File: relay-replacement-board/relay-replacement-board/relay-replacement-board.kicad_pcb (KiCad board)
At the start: 2 copper layers, 100 x 55 mm, 27 parts, among them J1 Conn_01x02, J10 Conn_01x02, J11 Conn_01x02, J12 Conn_01x02, J13 Conn_01x02, J2 Conn_01x02, J3 Conn_01x02, J4 Conn_01x02, J5 Conn_01x02, J6 Conn_01x02, J7 Conn_01x02, J8 Conn_01x02, J9 Conn_01x02, Q1 NVD5865NL, Q2 NVD5865NL, Q3 NVD5865NL, Q4 NVD5865NL, Q5 NVD5865NL, Q6 NVD5865NL, Q7 NVD5865NL

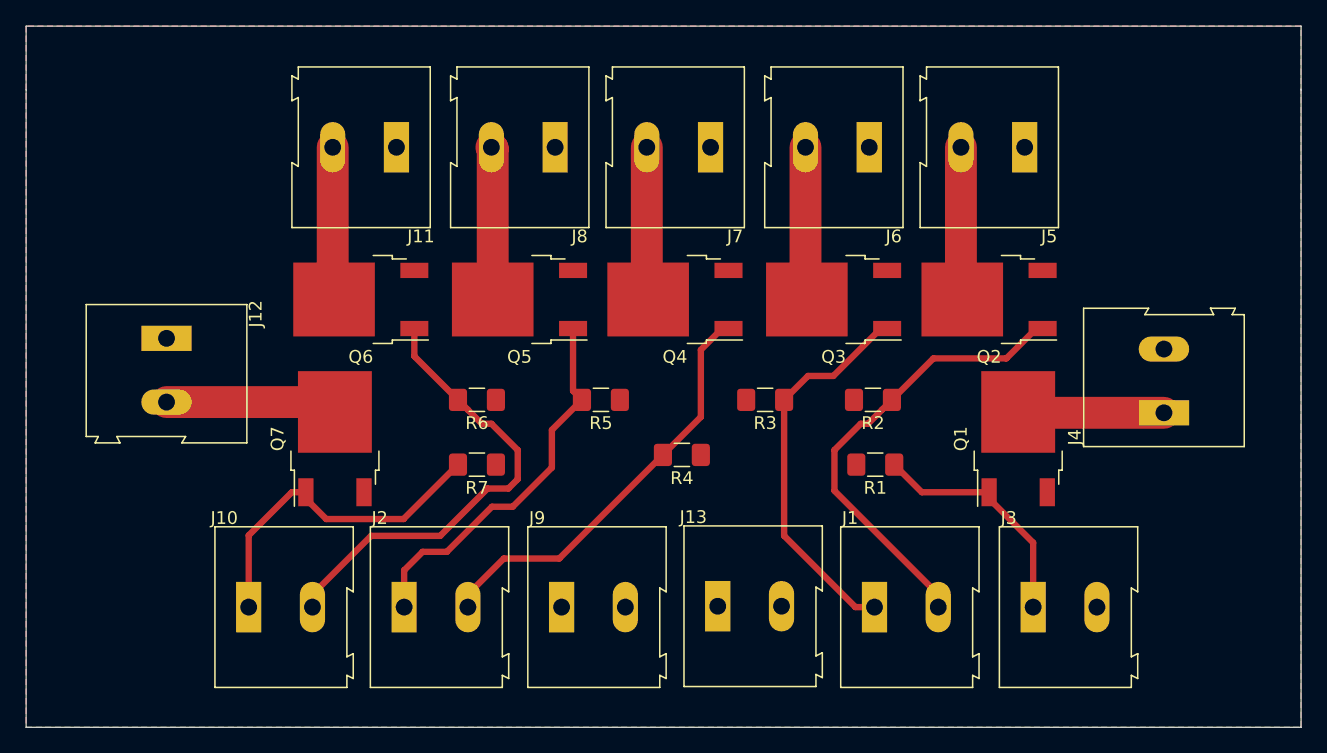
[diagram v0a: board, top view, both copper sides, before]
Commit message: Added flyback diodes
These protect the MOSFETs when they switch off. PCB also reorganised and shrunk slightly to 10*5cm
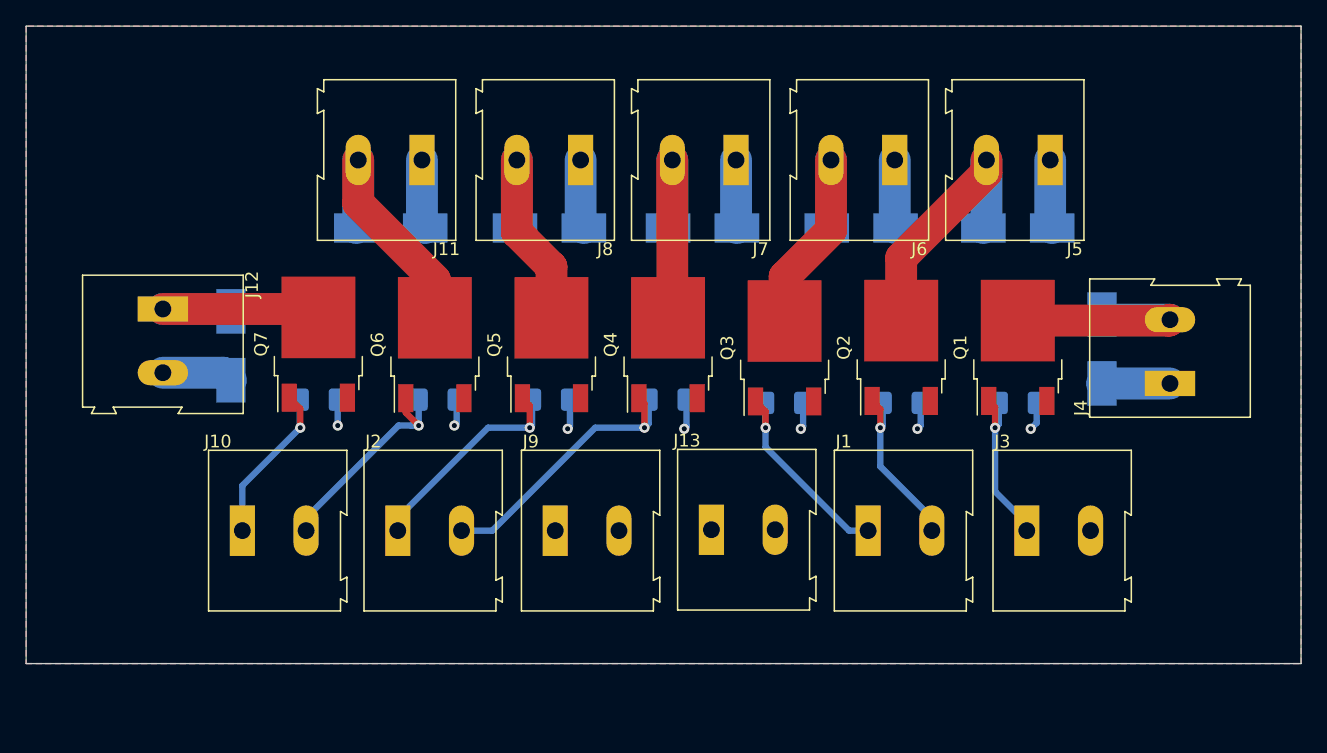
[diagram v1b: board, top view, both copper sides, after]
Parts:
- added D1: D, Diode_SMD:D_SMB_Handsoldering, B.Cu at (169.4, 95.3)
- added D2: D, Diode_SMD:D_SMB_Handsoldering, B.Cu at (162.8, 85.8)
- added D3: D, Diode_SMD:D_SMB_Handsoldering, B.Cu at (150.5, 85.8)
- added D4: D, Diode_SMD:D_SMB_Handsoldering, B.Cu at (138.1, 85.8)
- added D5: D, Diode_SMD:D_SMB_Handsoldering, B.Cu at (126.0, 85.8)
- added D6: D, Diode_SMD:D_SMB_Handsoldering, B.Cu at (113.6, 85.8)
- added D7: D, Diode_SMD:D_SMB_Handsoldering, B.Cu at (101.1, 95.1)
- R1, R2, R3, R4, R5, R6, R7: moved to B.Cu
- moved R7 13.4 mm to (108.0, 99.3)
- moved R1 12.2 mm to (162.8, 99.6)
- moved Q2 7.85 mm to (153.6, 95.2), turned to 90 degrees
- moved Q7 7.53 mm to (107.9, 94.9)
- moved Q1 7.16 mm to (162.8, 95.2)
- moved Q6 6.80 mm to (117.1, 95.0), turned to 90 degrees
- moved J1 6.02 mm to (151.0, 109.6)
- moved J10 6.02 mm to (102.0, 109.6)
- moved J13 6.02 mm to (138.8, 109.5)
- moved J2 6.02 mm to (114.2, 109.6)
- moved J3 6.02 mm to (163.5, 109.6)
- moved J9 6.02 mm to (126.5, 109.6)
- moved Q3 5.40 mm to (144.5, 95.2), turned to 90 degrees
- moved R4 4.48 mm to (135.3, 99.3)
- moved Q5 4.34 mm to (126.2, 95.0), turned to 90 degrees
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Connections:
- J12 pad 1: +12V -> Net-(D7-Pad2)
- J12 pad 2: Net-(J12-Pad2) -> +12V
- J4 pad 1: Net-(J4-Pad1) -> +12V
- J4 pad 2: +12V -> Net-(D1-Pad2)
- Q1 pad 2: Net-(J4-Pad1) -> Net-(D1-Pad2)
- Q7 pad 2: Net-(J12-Pad2) -> Net-(D7-Pad2)
- R1 pad 1: /trigger0 -> GND
- R1 pad 2: GND -> /trigger0
- R2 pad 1: /trigger1 -> GND
- R2 pad 2: GND -> /trigger1
- R3 pad 1: /trigger2 -> GND
- R3 pad 2: GND -> /trigger2
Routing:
- net +12V: track 0.00 -> 37.9 mm
- net /trigger1: track 36.0 -> 14.1 mm, vias 0 -> 1
- net /trigger5: track 36.5 -> 17.4 mm, vias 0 -> 1
- net Net-(D7-Pad2): track 0.00 -> 17.9 mm
- net Net-(D1-Pad2): track 0.00 -> 17.5 mm
- net GND: track 0.00 -> 15.3 mm, vias 0 -> 7
- net /trigger2: track 30.5 -> 16.6 mm, vias 0 -> 1
- net Net-(J12-Pad2): track 13.5 -> 0.00 mm
- net /trigger6: track 26.4 -> 14.9 mm, vias 0 -> 1
- net Net-(J4-Pad1): track 11.5 -> 0.00 mm
- net /trigger4: track 31.0 -> 20.1 mm, vias 0 -> 1
- net /trigger3: track 33.2 -> 22.5 mm, vias 0 -> 1
- net Net-(D2-Pad2): track 12.0 -> 20.8 mm
- net Net-(D6-Pad2): track 12.0 -> 20.3 mm
- net Net-(D3-Pad2): track 12.0 -> 19.8 mm
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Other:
- board size 100 x 55 mm -> 100 x 50 mm

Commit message: Added M4 mounting holes
THese are not currently connected to Ground but could be
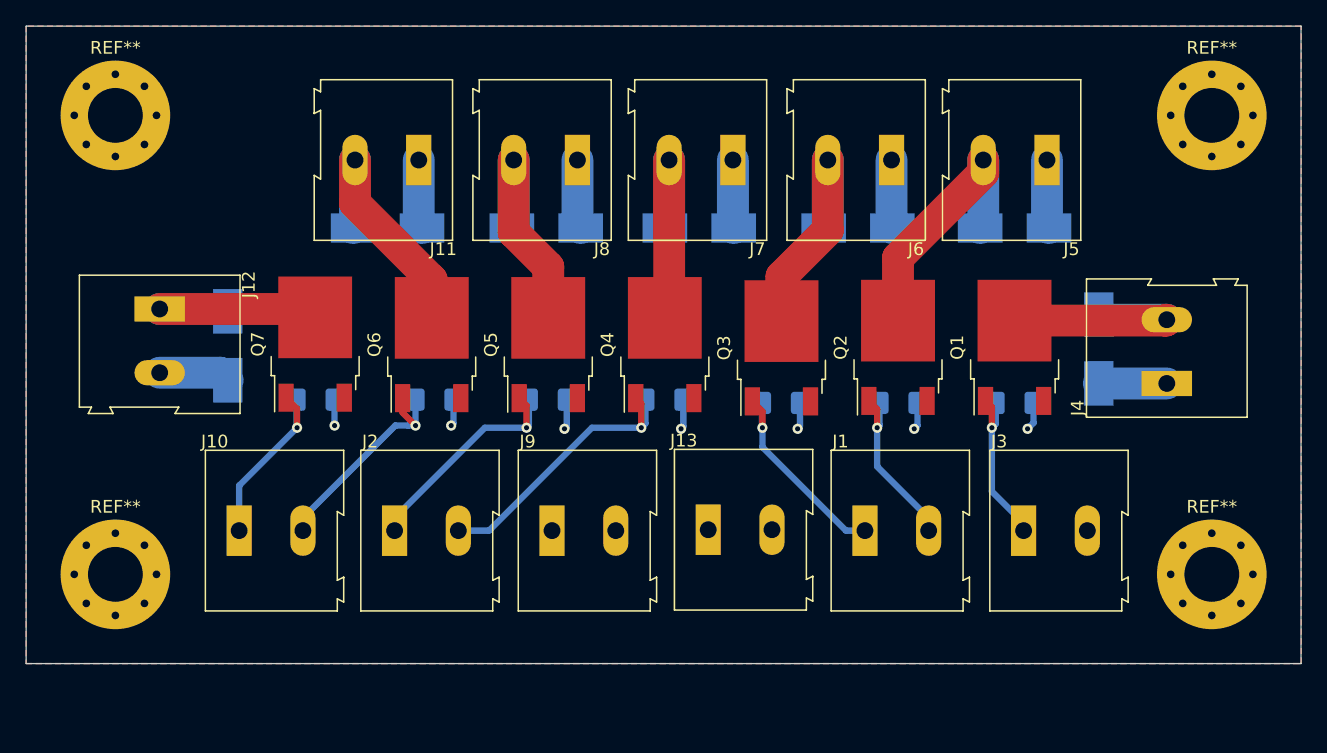
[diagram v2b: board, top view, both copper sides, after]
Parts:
- added REF**: MountingHole_4.3mm_M4_Pad_Via, MountingHole:MountingHole_4.3mm_M4_Pad_Via, F.Cu at (92.0, 77.0)
- added REF**: MountingHole_4.3mm_M4_Pad_Via, MountingHole:MountingHole_4.3mm_M4_Pad_Via, F.Cu at (178.0, 77.0)
- added REF**: MountingHole_4.3mm_M4_Pad_Via, MountingHole:MountingHole_4.3mm_M4_Pad_Via, F.Cu at (92.0, 113.0)
- added REF**: MountingHole_4.3mm_M4_Pad_Via, MountingHole:MountingHole_4.3mm_M4_Pad_Via, F.Cu at (178.0, 113.0)
- moved D1 0.25 mm to (169.1, 95.3)
- moved D2 0.25 mm to (162.5, 85.8)
- moved D3 0.25 mm to (150.2, 85.8)
- moved D4 0.25 mm to (137.8, 85.8)
- moved D5 0.25 mm to (125.8, 85.8)
- moved D6 0.25 mm to (113.3, 85.8)
- moved D7 0.25 mm to (100.8, 95.1)
- moved J1 0.25 mm to (150.8, 109.6)
- moved J10 0.25 mm to (101.7, 109.6)
- moved J11 0.25 mm to (115.8, 80.5)
- moved J12 0.25 mm to (95.5, 92.2)
- moved J13 0.25 mm to (138.5, 109.5)
- moved J2 0.25 mm to (113.9, 109.6)
- moved J3 0.25 mm to (163.2, 109.6)
- moved J4 0.25 mm to (174.5, 98.0)
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
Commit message: Added silkscreen
Text explaining what to connect where on the board
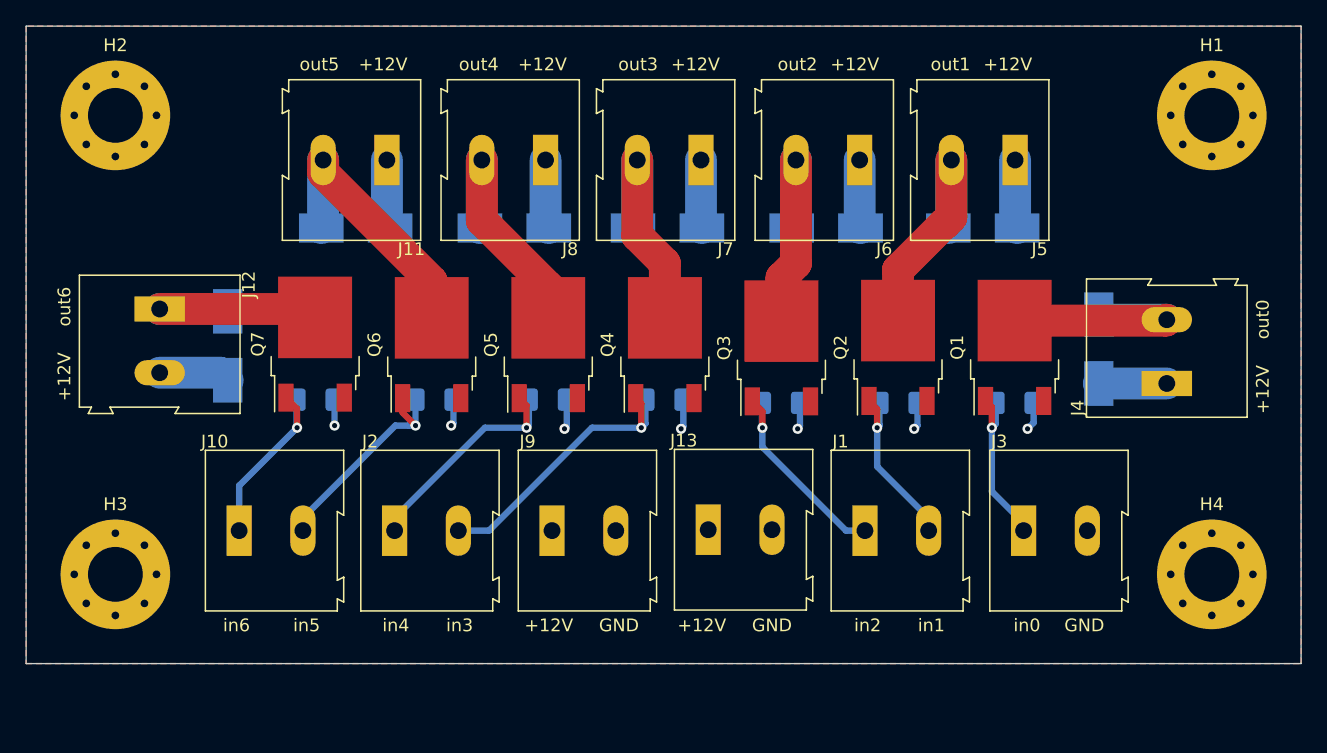
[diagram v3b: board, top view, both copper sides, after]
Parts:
- removed REF**: MountingHole_4.3mm_M4_Pad_Via, MountingHole:MountingHole_4.3mm_M4_Pad_Via
- added H2: MountingHole_4.3mm_M4_Pad_Via, MountingHole:MountingHole_4.3mm_M4_Pad_Via, F.Cu at (92.0, 77.0)
- moved D2 2.50 mm to (160.0, 85.8)
- moved D3 2.50 mm to (147.7, 85.8)
- moved D4 2.50 mm to (135.3, 85.8)
- moved D5 2.50 mm to (123.3, 85.8)
- moved D6 2.50 mm to (110.8, 85.8)
- moved J11 2.50 mm to (113.3, 80.5)
- moved J5 2.50 mm to (162.6, 80.5)
- moved J6 2.50 mm to (150.4, 80.5)
- moved J7 2.50 mm to (137.9, 80.5)
- moved J8 2.50 mm to (125.7, 80.5)
- renumbered REF** to H1, REF** to H3, REF** to H4
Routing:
- net Net-(D6-Pad2): track 20.3 -> 21.3 mm
- net Net-(D5-Pad2): track 18.9 -> 19.9 mm
- net Net-(D3-Pad2): track 19.8 -> 18.7 mm
- net Net-(D2-Pad2): track 20.8 -> 19.8 mm
- net Net-(D4-Pad2): track 18.0 -> 18.7 mm
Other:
- board text added: "+12V"
- board text added: "7xMOSFET relay replacement board University of Southampton SUSF Lunar Hopper Harry Snell 2019 Connect solenoid valve to +12V and outN"
- board text added: "GND"
- board text added: "in0"
- board text added: "in1"
- board text added: "in2"
- board text added: "in3"
- board text added: "in4"
- board text added: "in5"
- board text added: "in6"
- board text added: "out0"
- board text added: "out1"
- board text added: "out2"
- board text added: "out3"
- board text added: "out4"
- board text added: "out5"
- board text added: "out6"
- board text removed: "7xMOSFET relay replacement board University of Southampton SUSF Lunar Hopper Harry Snell 2019"
